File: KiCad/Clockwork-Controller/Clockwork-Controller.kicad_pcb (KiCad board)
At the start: 2 copper layers, 56.4 x 94.2 mm, 95 parts, among them CN2 PJ-307N5, J2 to DIN-6 Male, J3 Pause Button, J4 ICSP, J5 LED-Connector, Q1 AO3400A, Q2 SS8050, Q3 SS8050, Q4 SS8050, SW1 Guide/Follow, SW2 Mode -, SW3 Mode +, SW4 Frame -, SW5 Frame +, U1 ECS-TXO-3225MV-160-TR, U2 AP2210N-3.3TRG1, U3 74HCT14, U4 G3VM-61VY3(TR), U5 MCP4725, U6 LMC6482, U7 ATmega328P-A

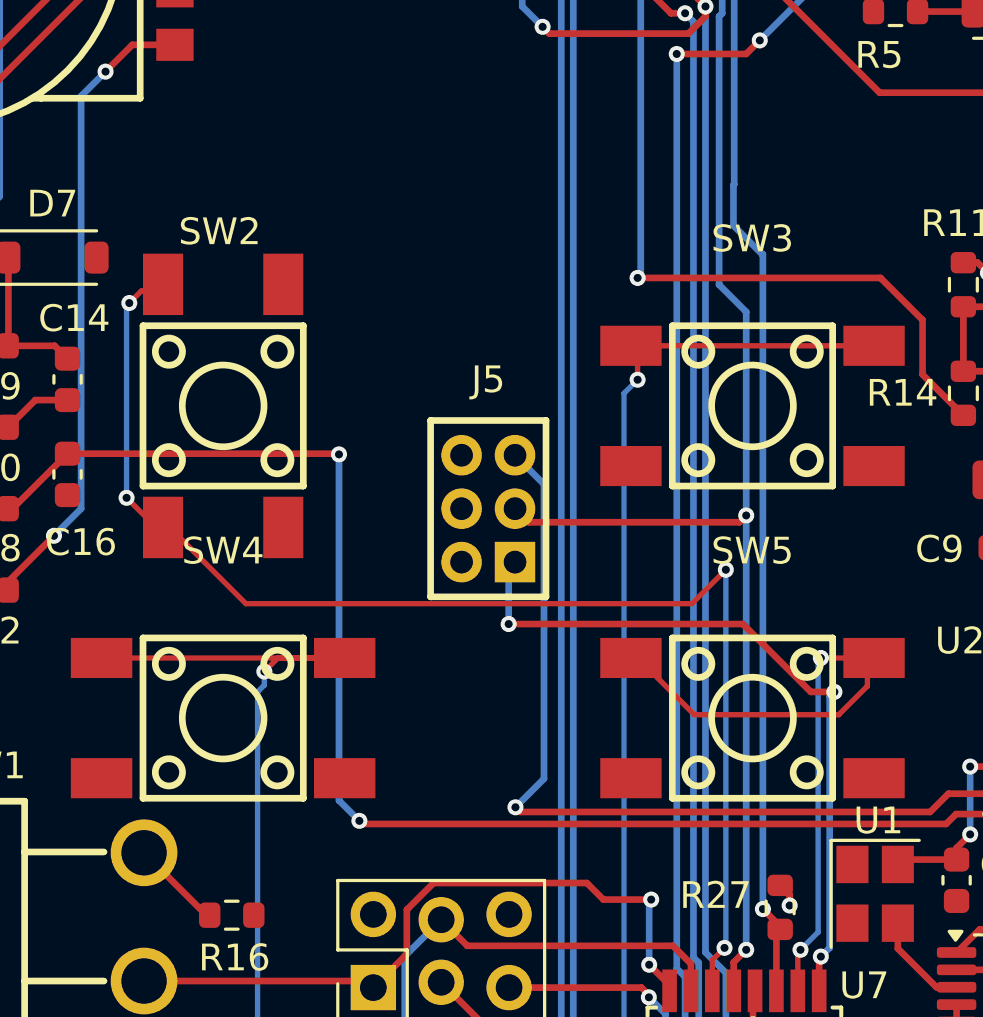
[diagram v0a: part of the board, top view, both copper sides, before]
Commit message: New Gerbers, added the xtal to the BOM, new MH for OLED
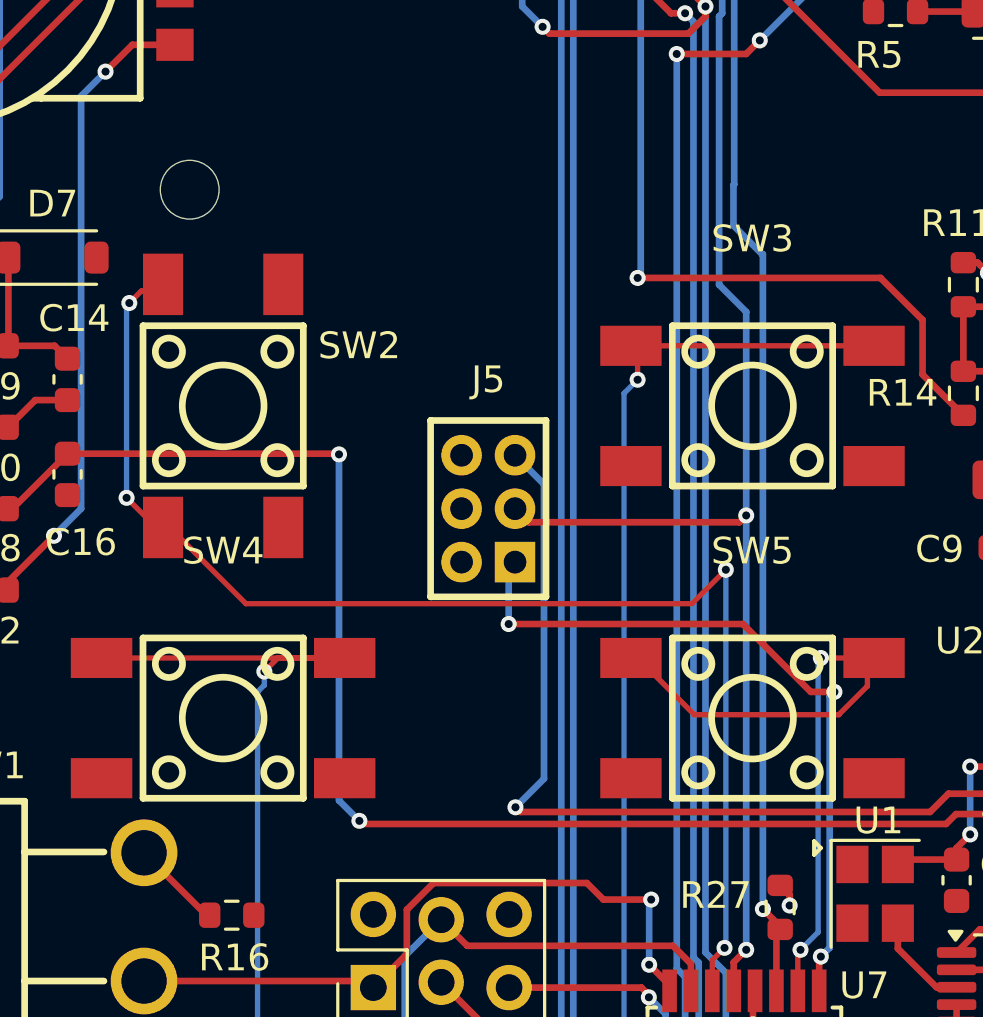
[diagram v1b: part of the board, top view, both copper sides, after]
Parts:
- added H2: MH Display, MountingHole:MountingHole_2.2mm_M2_DIN965, F.Cu at (55.4, 68.3)

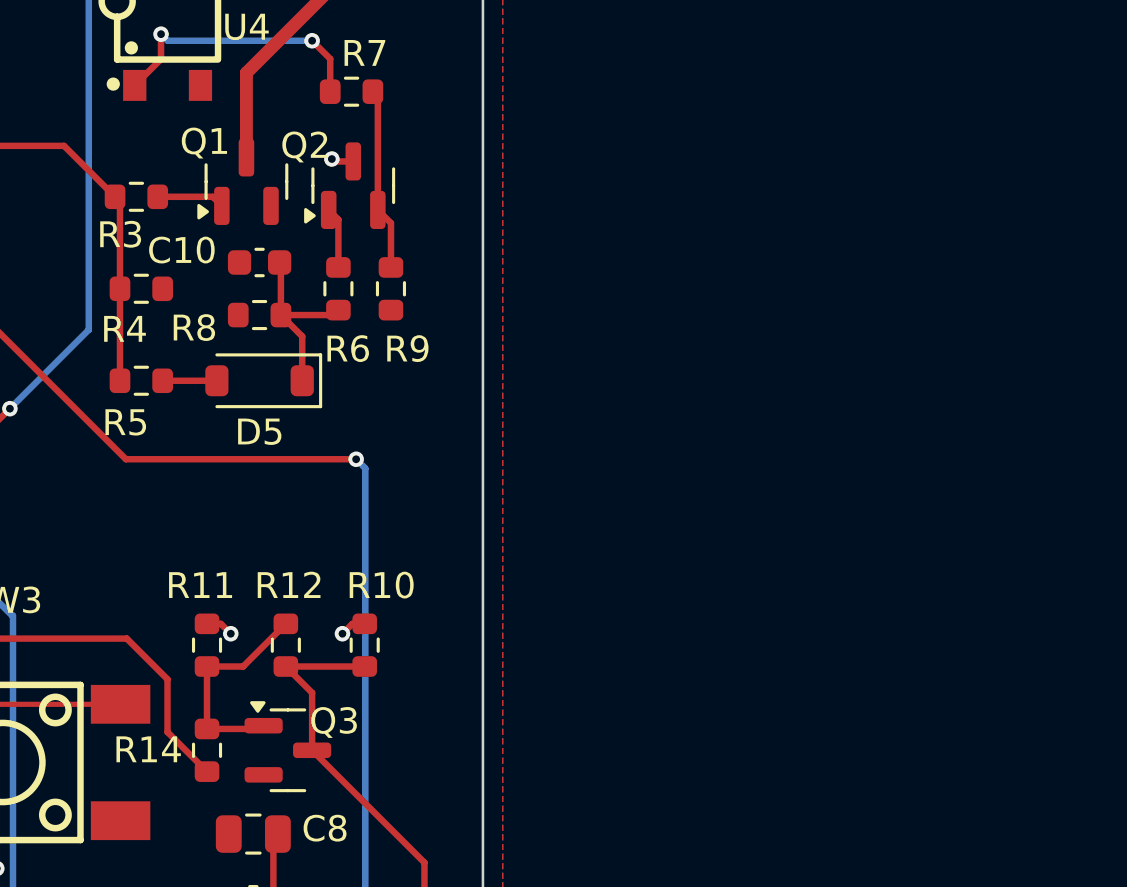
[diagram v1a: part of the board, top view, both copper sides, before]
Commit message: Removing redundant R11, pulling M Pin up before reaching the Schmitt Triggers
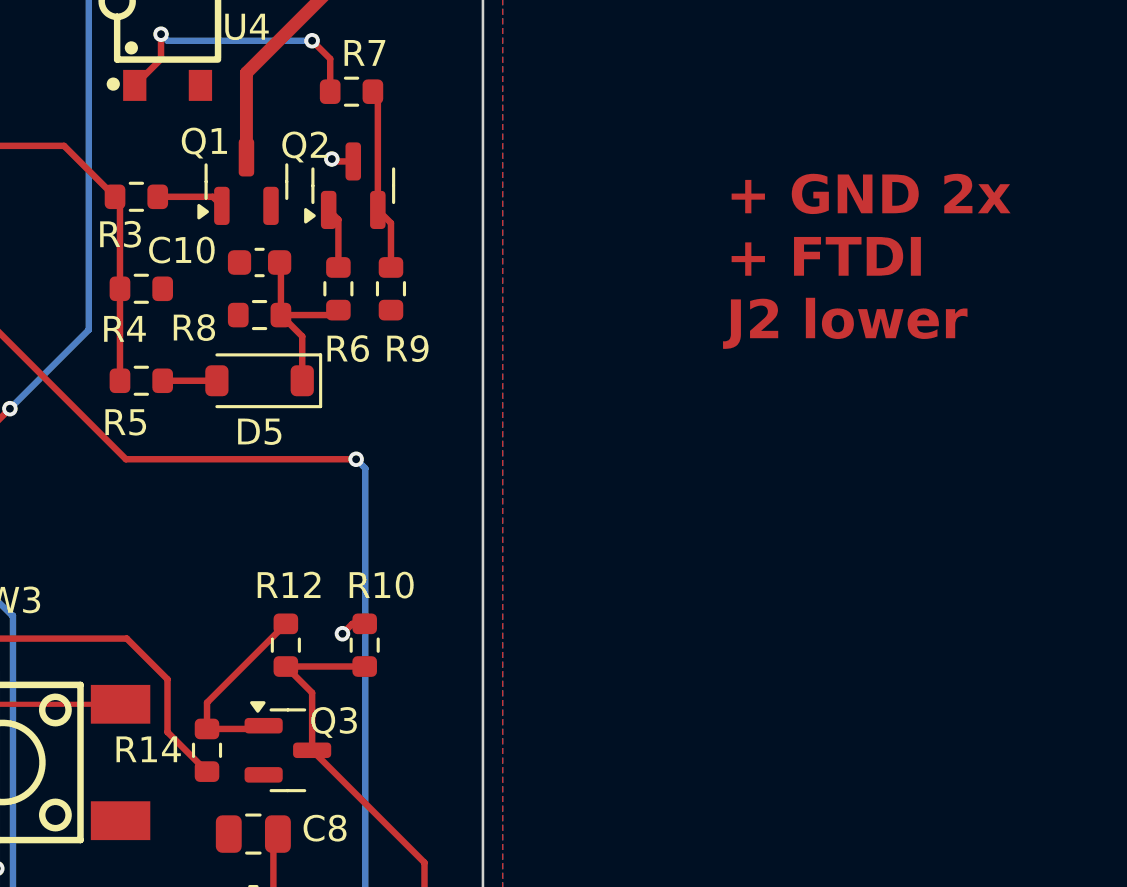
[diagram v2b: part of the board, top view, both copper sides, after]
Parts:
- removed R11: 47k, Resistor_SMD:R_0603_1608Metric
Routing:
- net +5V: track 67.7 -> 66.7 mm, vias 22 -> 21
- net Net-(Q3-B): track 8.39 -> 7.57 mm
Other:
- board text added: "+ GND 2x + FTDI J2 lower"

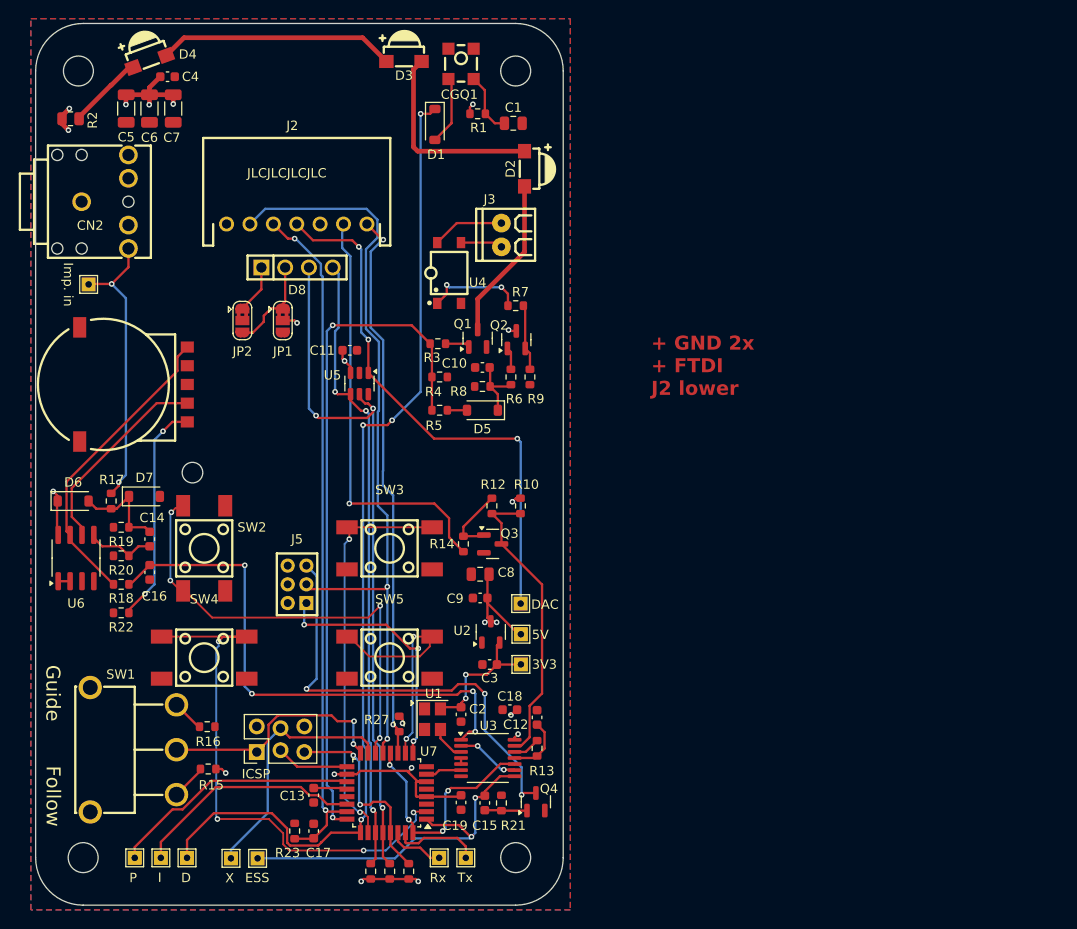
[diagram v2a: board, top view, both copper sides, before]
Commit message: Swao Ext.Imp and Sync LED
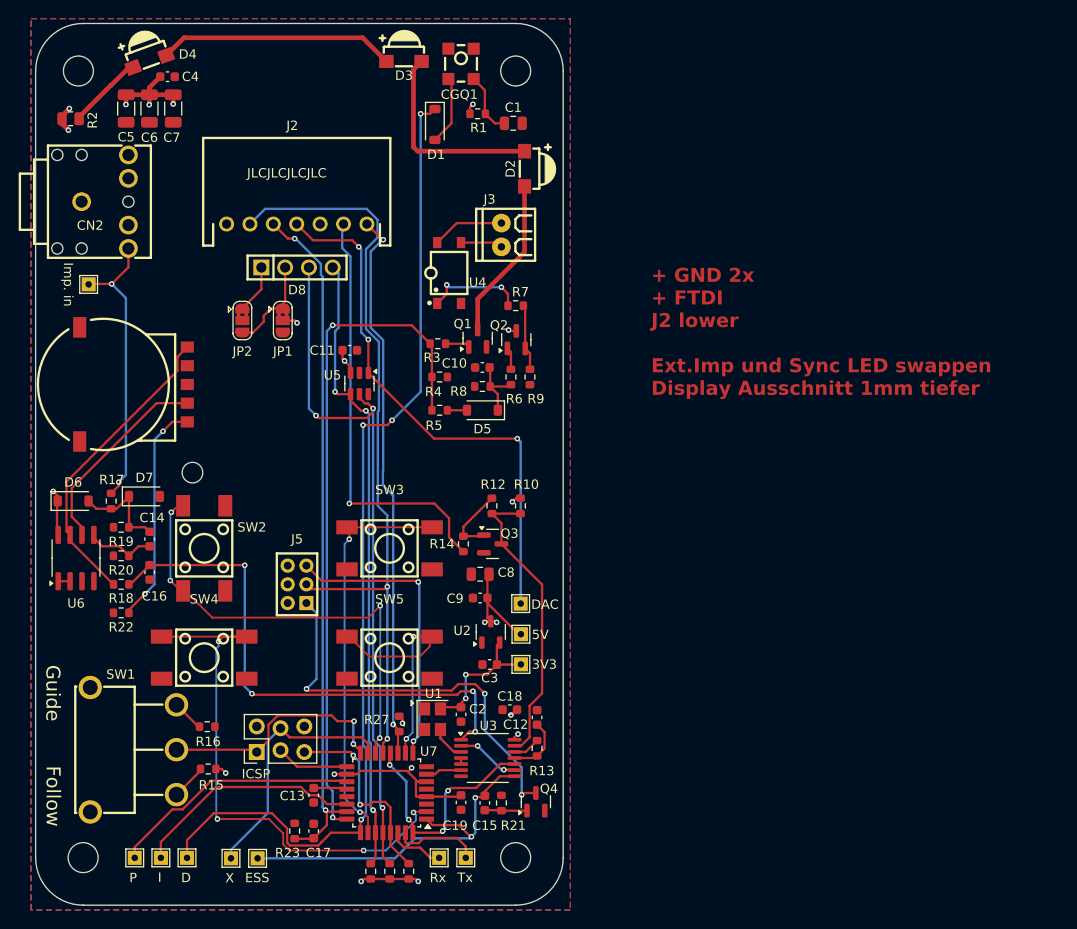
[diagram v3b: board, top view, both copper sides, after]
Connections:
- J5 pad 1: /In_Sync-LED -> /Ext_Imp_LED
- J5 pad 5: /Ext_Imp_LED -> /In_Sync-LED
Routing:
- net /In_Sync-LED: track 27.4 -> 31.3 mm, vias 3 -> 2
- net /Ext_Imp_LED: track 48.0 -> 44.6 mm
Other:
- board text added: "+ GND 2x + FTDI J2 lower Ext.Imp und Sync LED swappen Display Ausschnitt 1mm tiefer"
- board text removed: "+ GND 2x + FTDI J2 lower"
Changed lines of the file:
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@@
 			(layers "*.Cu" "*.Mask")
 			(remove_unused_layers no)
-			(net 27 "/In_Sync-LED")
+			(net 26 "/Ext_Imp_LED")
 			(pinfunction "1")
 			(pintype "passive")
@@
 			(layers "*.Cu" "*.Mask")
 			(remove_unused_layers no)
-			(net 26 "/Ext_Imp_LED")
+			(net 27 "/In_Sync-LED")
 			(pinfunction "5")
 			(pintype "passive")
@@
 		(layer "Edge.Cuts")
 	)
-	(gr_text "+ GND 2x\n+ FTDI\nJ2 lower"
+	(gr_text "+ GND 2x\n+ FTDI\nJ2 lower\n\nExt.Imp und Sync LED swappen\nDisplay Ausschnitt 1mm tiefer"
 		(at 104.394 60.198 0)
 		(layer "F.Cu")
@@
 	)
 	(segment
+		(start 67.31 82.502)
+		(end 67.548 82.264)
+		(width 0.25)
+		(layer "F.Cu")
+		(net 26)
+	)
+	(segment
 		(start 90.7519 102.5675)
 		(end 92.075 102.5675)
@@
 	)
 	(segment
-		(start 67.548 78.264)
-		(end 68.633 79.349)
+		(start 67.31 82.502)
+		(end 67.548 82.264)
+		(width 0.25)
+		(layer "B.Cu")
+		(net 26)
+	)
+	(segment
+		(start 68.633 90.371)
+		(end 67.564 91.44)
 		(width 0.25)
 		(layer "B.Cu")
@@
 	)
 	(segment
-		(start 68.633 79.349)
-		(end 68.633 90.371)
+		(start 67.548 82.264)
+		(end 68.633 83.349)
 		(width 0.25)
 		(layer "B.Cu")
@@
 	)
 	(segment
-		(start 68.633 90.371)
-		(end 67.564 91.44)
+		(start 68.633 83.349)
+		(end 68.633 90.371)
 		(width 0.25)
 		(layer "B.Cu")
@@
 	)
 	(segment
-		(start 78.932 98.309)
-		(end 78.932 97.09)
+		(start 79.385 79.893)
+		(end 69.177 79.893)
 		(width 0.25)
 		(layer "F.Cu")
@@
 	)
 	(segment
-		(start 79.502 87.122)
-		(end 78.618116 87.122)
-		(width 0.25)
-		(layer "F.Cu")
-		(net 27)
-	)
-	(segment
-		(start 76.078116 84.582)
-		(end 67.31 84.582)
+		(start 78.932 98.309)
+		(end 78.932 97.09)
 		(width 0.25)
 		(layer "F.Cu")
@@
 	)
 	(segment
-		(start 78.618116 87.122)
-		(end 76.078116 84.582)
+		(start 79.502 80.01)
+		(end 79.385 79.893)
 		(width 0.25)
 		(layer "F.Cu")
@@
 	)
 	(segment
-		(start 67.31 82.502)
-		(end 67.548 82.264)
+		(start 69.177 79.893)
+		(end 67.548 78.264)
 		(width 0.25)
 		(layer "F.Cu")
@@
 	)
 	(via
-		(at 67.31 84.582)
-		(size 0.6)
-		(drill 0.3)
-		(layers "F.Cu" "B.Cu")
-		(net 27)
-	)
-	(via
-		(at 79.502 87.122)
+		(at 79.502 80.01)
 		(size 0.6)
 		(drill 0.3)
@@
 	)
 	(segment
-		(start 67.31 82.502)
-		(end 67.548 82.264)
+		(start 79.502 80.01)
+		(end 79.619 80.127)
 		(width 0.25)
 		(layer "B.Cu")
@@
 	)
 	(segment
-		(start 79.3242 96.6978)
+		(start 79.619 96.403)
 		(end 78.994 97.028)
 		(width 0.25)
@@
 	)
 	(segment
-		(start 79.502 87.122)
-		(end 79.3242 87.2998)
-		(width 0.25)
-		(layer "B.Cu")
-		(net 27)
-	)
-	(segment
-		(start 79.3242 87.2998)
-		(end 79.3242 96.6978)
-		(width 0.25)
-		(layer "B.Cu")
-		(net 27)
-	)
-	(segment
-		(start 67.31 84.582)
-		(end 67.31 82.502)
+		(start 79.619 80.127)
+		(end 79.619 96.403)
 		(width 0.25)
 		(layer "B.Cu")

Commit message: Adding GND TPs
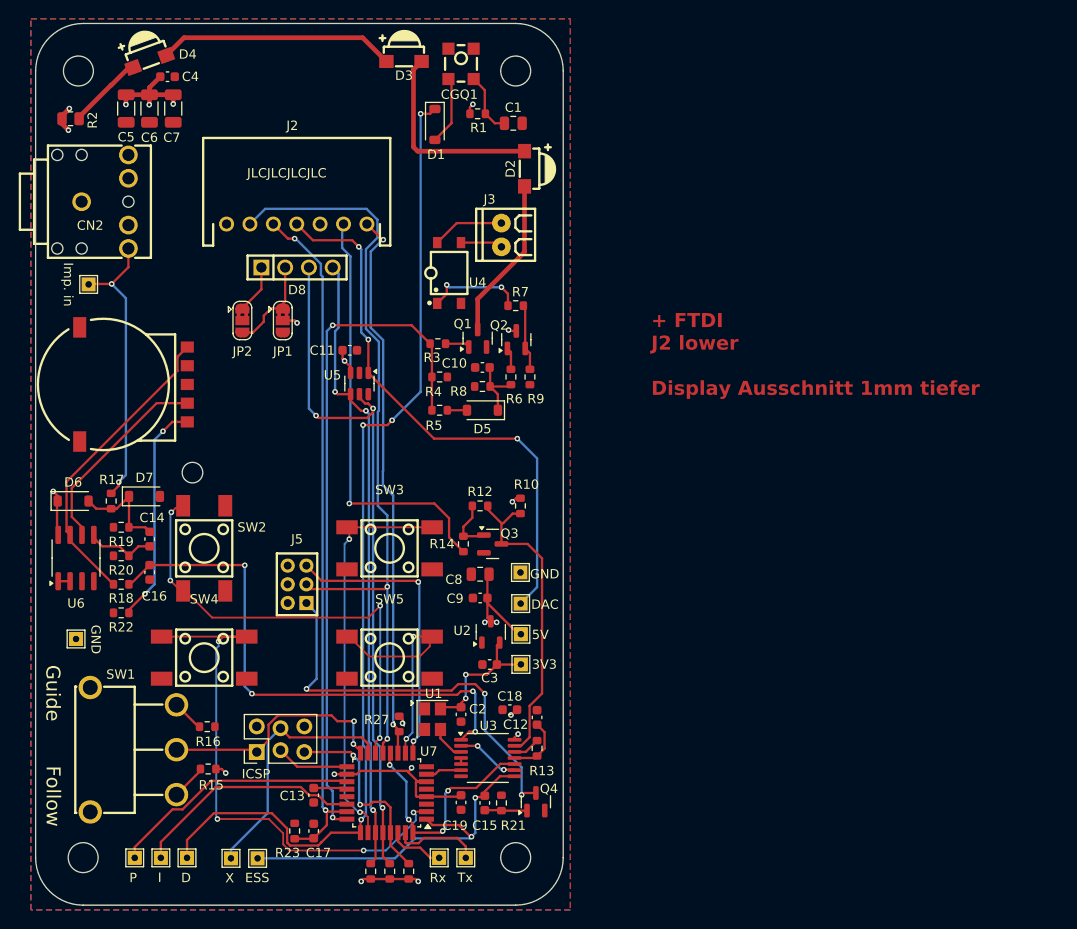
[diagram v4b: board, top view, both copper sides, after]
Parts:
- added TP3: GND, TestPoint:TestPoint_THTPad_1.5x1.5mm_Drill0.7mm, F.Cu at (42.9, 86.1)
- added TP4: GND, TestPoint:TestPoint_THTPad_1.5x1.5mm_Drill0.7mm, F.Cu at (90.4, 79.0)
- moved R12 1.27 mm to (86.1, 71.9), turned to 0 degrees
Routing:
- net Net-(Q3-C): track 31.7 -> 33.8 mm
- net Net-(Q3-B): track 7.57 -> 5.87 mm
- net /Ctrl_V: track 58.2 -> 59.6 mm
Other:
- board text added: "+ FTDI J2 lower Display Ausschnitt 1mm tiefer"
- board text added: "GND"
- board text removed: "+ GND 2x + FTDI J2 lower Ext.Imp und Sync LED swappen Display Ausschnitt 1mm tiefer"
